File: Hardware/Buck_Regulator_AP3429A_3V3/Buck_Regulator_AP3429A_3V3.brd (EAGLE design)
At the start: 25.4 x 25.4 mm, 51 parts, among them J1 Screw Terminal, J2 POWER_JACKPOWER_JACK_SLOT_COM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, J3 Breakout Headers, U1 AP3429/A

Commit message: Added correct measurements
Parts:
- moved FRAME1 24.4 mm to (-14.0, -41.9)
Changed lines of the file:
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@@
 <layer number="45" name="Holes" color="7" fill="1" visible="yes" active="yes"/>
 <layer number="46" name="Milling" color="3" fill="1" visible="no" active="yes"/>
-<layer number="47" name="Measures" color="7" fill="1" visible="no" active="yes"/>
+<layer number="47" name="Measures" color="7" fill="1" visible="yes" active="yes"/>
 <layer number="48" name="Document" color="7" fill="1" visible="no" active="yes"/>
 <layer number="49" name="Reference" color="7" fill="1" visible="no" active="yes"/>
@@
 <wire x1="7.366" y1="10.541" x2="7.62" y2="10.287" width="0.1778" layer="21"/>
 <text x="20.447" y="0.508" size="1.778" layer="16" font="vector" ratio="15" rot="MR0">v01</text>
-<text x="16.51" y="-17.78" size="1.778" layer="51" font="vector" ratio="10" distance="15">M. Chodikov</text>
+<text x="12.7" y="-41.91" size="1.778" layer="51" font="vector" ratio="10" distance="15">M. Chodikov</text>
 <text x="5.08" y="46.99" size="1.778" layer="47" font="vector" ratio="15">Units in Inches</text>
 <wire x1="5.334" y1="11.176" x2="5.334" y2="10.414" width="0.2032" layer="22"/>
@@
 <rectangle x1="6.35" y1="3.81" x2="21.59" y2="16.51" layer="30" rot="R180"/>
 <wire x1="5.08" y1="11.43" x2="5.334" y2="11.176" width="0.2032" layer="22"/>
-<dimension x1="25.4" y1="25.4" x2="22.86" y2="25.4" x3="24.13" y3="29.21" textsize="1.778" textratio="15" layer="47" unit="inch"/>
-<dimension x1="2.54" y1="22.86" x2="0" y2="22.86" x3="1.27" y3="35.56" textsize="1.778" textratio="15" layer="47" unit="inch"/>
-<dimension x1="25.4" y1="25.4" x2="0" y2="25.4" x3="12.7" y3="40.64" textsize="1.778" textratio="15" layer="47" unit="inch"/>
-<dimension x1="2.54" y1="2.54" x2="2.54" y2="0" x3="-2.54" y3="1.27" textsize="1.778" textratio="15" layer="47" unit="inch"/>
-<dimension x1="2.54" y1="22.86" x2="2.54" y2="25.4" x3="-2.54" y3="24.13" textsize="1.778" textratio="15" layer="47" unit="inch"/>
-<dimension x1="3.683" y1="7.28" x2="3.81" y2="0" x3="-8.89" y3="3.64" textsize="1.778" textratio="15" layer="47" dtype="vertical" unit="inch"/>
-<dimension x1="3.683" y1="7.28" x2="3.81" y2="10.795" x3="-13.97" y3="9.0375" textsize="1.778" textratio="15" layer="47" dtype="vertical" unit="inch"/>
-<dimension x1="0" y1="25.4" x2="0" y2="0" x3="-20.32" y3="12.7" textsize="1.778" textratio="15" layer="47" unit="inch"/>
-<dimension x1="24.13" y1="7.493" x2="24.13" y2="0" x3="30.48" y3="3.7465" textsize="1.778" textratio="15" layer="47" unit="inch"/>
-<dimension x1="24.13" y1="7.62" x2="24.13" y2="10.16" x3="30.48" y3="8.89" textsize="1.778" textratio="15" layer="47" unit="inch"/>
+<dimension x1="2.54" y1="2.54" x2="0" y2="2.54" x3="1.27" y3="-3.81" textsize="1.778" textratio="15" layer="47" unit="inch"/>
+<dimension x1="3.683" y1="17.78" x2="0" y2="17.78" x3="1.8415" y3="-7.62" textsize="1.778" textratio="15" layer="47" unit="inch"/>
+<dimension x1="13.335" y1="24.003" x2="0" y2="24.003" x3="6.6675" y3="-12.7" textsize="1.778" textratio="15" layer="47" unit="inch"/>
+<dimension x1="22.86" y1="2.54" x2="0" y2="2.54" x3="11.43" y3="-17.78" textsize="1.778" textratio="15" layer="47" unit="inch"/>
+<dimension x1="24.13" y1="7.62" x2="0" y2="7.62" x3="12.065" y3="-21.59" textsize="1.778" textratio="15" layer="47" unit="inch"/>
+<dimension x1="25.4" y1="0" x2="0" y2="0" x3="12.7" y3="-26.67" textsize="1.778" textratio="15" layer="47" unit="inch"/>
+<dimension x1="3.683" y1="7.28" x2="3.81" y2="0" x3="-1.651" y3="3.64" textsize="1.778" textratio="15" layer="47" dtype="vertical" unit="inch"/>
+<dimension x1="24.13" y1="7.62" x2="24.13" y2="0" x3="-5.334" y3="3.81" textsize="1.778" textratio="15" layer="47" dtype="vertical" unit="inch"/>
+<dimension x1="25.4" y1="0" x2="24.13" y2="10.16" x3="-9.271" y3="5.08" textsize="1.778" textratio="15" layer="47" dtype="vertical" unit="inch"/>
+<dimension x1="3.683" y1="10.795" x2="3.683" y2="0" x3="-12.827" y3="5.3975" textsize="1.778" textratio="15" layer="47" dtype="vertical" unit="inch"/>
+<dimension x1="2.54" y1="2.54" x2="2.54" y2="0" x3="-16.51" y3="1.27" textsize="1.778" textratio="15" layer="47" dtype="vertical" unit="inch"/>
+<dimension x1="2.54" y1="22.86" x2="2.54" y2="0" x3="-20.32" y3="11.43" textsize="1.778" textratio="15" layer="47" dtype="vertical" unit="inch"/>
+<dimension x1="13.335" y1="24.003" x2="13.97" y2="0" x3="-25.4" y3="12.0015" textsize="1.778" textratio="15" layer="47" dtype="vertical" unit="inch"/>
+<dimension x1="0" y1="0" x2="0" y2="25.4" x3="-29.21" y3="12.7" textsize="1.778" textratio="15" layer="47" dtype="vertical" unit="inch"/>
+<text x="-25.4" y="-12.7" size="1.778" layer="47" font="vector" ratio="15">Units in Inches</text>
 </plain>
 <attributes>
@@
 <element name="FD3" library="SparkFun-Aesthetics" package="FIDUCIAL-MICRO" value="FIDUCIALUFIDUCIAL" x="0.762" y="24.638" smashed="yes" rot="MR0"/>
 <element name="FD4" library="SparkFun-Aesthetics" package="FIDUCIAL-MICRO" value="FIDUCIALUFIDUCIAL" x="0.762" y="24.638" smashed="yes"/>
-<element name="FRAME1" library="SparkFun-Aesthetics" package="CREATIVE_COMMONS" value="FRAME-LEDGER" x="-10.16" y="-17.78" smashed="yes">
-<attribute name="DESIGNER" value="M. Chodikov" x="69.85" y="-30.48" size="1.778" layer="27" display="off"/>
-<attribute name="REV" value="v01" x="69.85" y="-30.48" size="1.778" layer="27" display="off"/>
+<element name="FRAME1" library="SparkFun-Aesthetics" package="CREATIVE_COMMONS" value="FRAME-LEDGER" x="-13.97" y="-41.91" smashed="yes">
+<attribute name="DESIGNER" value="M. Chodikov" x="66.04" y="-54.61" size="1.778" layer="27" display="off"/>
+<attribute name="REV" value="v01" x="66.04" y="-54.61" size="1.778" layer="27" display="off"/>
 </element>
 <element name="L1" library="SparkFun-Coils" package="INDUCTOR_4X4MM" value="2.2μH" x="16.256" y="8.509" smashed="yes">

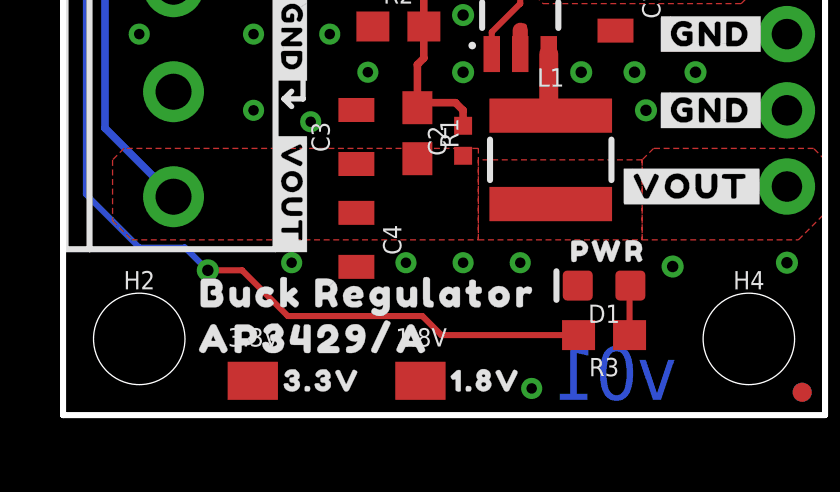
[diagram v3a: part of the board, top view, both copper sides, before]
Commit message: Further design review changes - v01
Added selective solder path to Document layer for the terminal block; moved the silkscreen name on the front to not be covered by the mounting hole anymore when a user uses a screw; nudges the LED power trace over for better GND connection; added measures to thermal pad (in reference to bottom right, and for the size)
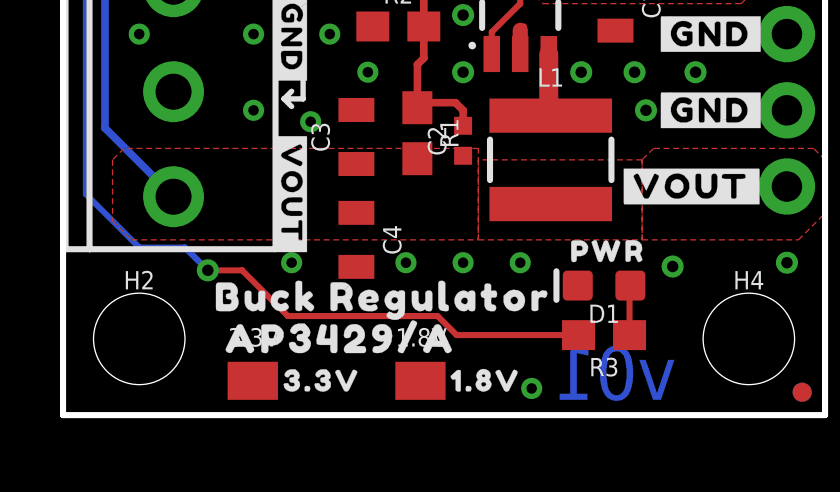
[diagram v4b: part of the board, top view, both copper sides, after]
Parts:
- moved U$3 0.89 mm to (9.27, 2.54)
- moved U$2 0.52 mm to (10.7, 3.94)
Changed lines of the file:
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@@
 <drawing>
 <settings>
-<setting alwaysvectorfont="no"/>
+<setting alwaysvectorfont="yes"/>
 <setting verticaltext="up"/>
 </settings>
@@
 <layer number="28" name="bValues" color="7" fill="1" visible="no" active="yes"/>
 <layer number="29" name="tStop" color="7" fill="3" visible="no" active="yes"/>
-<layer number="30" name="bStop" color="7" fill="6" visible="no" active="yes"/>
+<layer number="30" name="bStop" color="7" fill="6" visible="yes" active="yes"/>
 <layer number="31" name="tCream" color="7" fill="4" visible="no" active="yes"/>
 <layer number="32" name="bCream" color="7" fill="5" visible="no" active="yes"/>
@@
 <layer number="46" name="Milling" color="3" fill="1" visible="no" active="yes"/>
 <layer number="47" name="Measures" color="7" fill="1" visible="yes" active="yes"/>
-<layer number="48" name="Document" color="7" fill="1" visible="no" active="yes"/>
+<layer number="48" name="Document" color="7" fill="1" visible="yes" active="yes"/>
 <layer number="49" name="Reference" color="7" fill="1" visible="no" active="yes"/>
 <layer number="50" name="dxf" color="7" fill="1" visible="no" active="no"/>
@@
 <text x="20.447" y="0.508" size="1.778" layer="16" font="vector" ratio="15" rot="MR0">v01</text>
 <text x="12.7" y="-41.91" size="1.778" layer="51" font="vector" ratio="10" distance="15">M. Chodikov</text>
-<text x="5.08" y="46.99" size="1.778" layer="47" font="vector" ratio="15">Units in Inches</text>
 <wire x1="5.334" y1="11.176" x2="5.334" y2="10.414" width="0.2032" layer="22"/>
 <wire x1="5.334" y1="10.414" x2="4.826" y2="10.414" width="0.2032" layer="22"/>
@@
 <dimension x1="2.54" y1="2.54" x2="0" y2="2.54" x3="1.27" y3="-3.81" textsize="1.778" textratio="15" layer="47" unit="inch"/>
 <dimension x1="3.683" y1="17.78" x2="0" y2="17.78" x3="1.8415" y3="-7.62" textsize="1.778" textratio="15" layer="47" unit="inch"/>
-<dimension x1="13.335" y1="24.003" x2="0" y2="24.003" x3="6.6675" y3="-12.7" textsize="1.778" textratio="15" layer="47" unit="inch"/>
-<dimension x1="22.86" y1="2.54" x2="0" y2="2.54" x3="11.43" y3="-17.78" textsize="1.778" textratio="15" layer="47" unit="inch"/>
-<dimension x1="24.13" y1="7.62" x2="0" y2="7.62" x3="12.065" y3="-21.59" textsize="1.778" textratio="15" layer="47" unit="inch"/>
-<dimension x1="25.4" y1="0" x2="0" y2="0" x3="12.7" y3="-26.67" textsize="1.778" textratio="15" layer="47" unit="inch"/>
 <dimension x1="3.683" y1="7.28" x2="3.81" y2="0" x3="-1.651" y3="3.64" textsize="1.778" textratio="15" layer="47" dtype="vertical" unit="inch"/>
 <dimension x1="24.13" y1="7.62" x2="24.13" y2="0" x3="-5.334" y3="3.81" textsize="1.778" textratio="15" layer="47" dtype="vertical" unit="inch"/>
 <dimension x1="25.4" y1="0" x2="24.13" y2="10.16" x3="-9.271" y3="5.08" textsize="1.778" textratio="15" layer="47" dtype="vertical" unit="inch"/>
 <dimension x1="3.683" y1="10.795" x2="3.683" y2="0" x3="-12.827" y3="5.3975" textsize="1.778" textratio="15" layer="47" dtype="vertical" unit="inch"/>
-<dimension x1="2.54" y1="2.54" x2="2.54" y2="0" x3="-16.51" y3="1.27" textsize="1.778" textratio="15" layer="47" dtype="vertical" unit="inch"/>
-<dimension x1="2.54" y1="22.86" x2="2.54" y2="0" x3="-20.32" y3="11.43" textsize="1.778" textratio="15" layer="47" dtype="vertical" unit="inch"/>
-<dimension x1="13.335" y1="24.003" x2="13.97" y2="0" x3="-25.4" y3="12.0015" textsize="1.778" textratio="15" layer="47" dtype="vertical" unit="inch"/>
-<dimension x1="0" y1="0" x2="0" y2="25.4" x3="-29.21" y3="12.7" textsize="1.778" textratio="15" layer="47" dtype="vertical" unit="inch"/>
 <text x="-25.4" y="-12.7" size="1.778" layer="47" font="vector" ratio="15">Units in Inches</text>
+<wire x1="3.048" y1="16.891" x2="3.048" y2="6.35" width="5.9944" layer="48"/>
+<wire x1="3.048" y1="6.35" x2="0" y2="3.302" width="5.9944" layer="48"/>
+<dimension x1="6.35" y1="3.81" x2="0" y2="3.81" x3="3.175" y3="-11.43" textsize="1.778" textratio="15" layer="47" unit="inch"/>
+<dimension x1="13.335" y1="24.003" x2="0" y2="24.003" x3="6.6675" y3="-16.51" textsize="1.778" textratio="15" layer="47" unit="inch"/>
+<dimension x1="22.86" y1="2.54" x2="0" y2="2.54" x3="11.43" y3="-21.59" textsize="1.778" textratio="15" layer="47" unit="inch"/>
+<dimension x1="24.13" y1="7.62" x2="0" y2="7.62" x3="12.065" y3="-25.4" textsize="1.778" textratio="15" layer="47" unit="inch"/>
+<dimension x1="25.4" y1="0" x2="0" y2="0" x3="12.7" y3="-29.21" textsize="1.778" textratio="15" layer="47" unit="inch"/>
+<dimension x1="6.35" y1="3.81" x2="6.35" y2="0" x3="-16.51" y3="1.905" textsize="1.778" textratio="15" layer="47" unit="inch"/>
+<dimension x1="2.54" y1="2.54" x2="2.54" y2="0" x3="-20.32" y3="1.27" textsize="1.778" textratio="15" layer="47" unit="inch"/>
+<dimension x1="2.54" y1="22.86" x2="2.54" y2="0" x3="-24.13" y3="11.43" textsize="1.778" textratio="15" layer="47" unit="inch"/>
+<dimension x1="13.335" y1="24.003" x2="13.335" y2="0" x3="-27.94" y3="12.0015" textsize="1.778" textratio="15" layer="47" unit="inch"/>
+<dimension x1="0" y1="0" x2="0" y2="25.4" x3="-31.75" y3="12.7" textsize="1.778" textratio="15" layer="47" unit="inch"/>
+<dimension x1="21.59" y1="3.81" x2="21.59" y2="16.51" x3="30.48" y3="10.16" textsize="1.778" textratio="15" layer="47" unit="inch"/>
+<dimension x1="6.35" y1="16.51" x2="21.59" y2="16.51" x3="13.97" y3="35.56" textsize="1.778" textratio="15" layer="47" unit="inch"/>
 </plain>
 <attributes>
@@
 <attribute name="VALUE" x="22.098" y="19.05" size="0.6096" layer="27" font="vector" ratio="20" rot="R270"/>
 </element>
-<element name="U$2" library="output" package="BUCK_REGULATOR24" value="" x="10.16" y="4.064" smashed="yes"/>
-<element name="U$3" library="output" package="AP3429#A25" value="" x="8.382" y="2.54" smashed="yes"/>
+<element name="U$2" library="output" package="BUCK_REGULATOR24" value="" x="10.668" y="3.937" smashed="yes"/>
+<element name="U$3" library="output" package="AP3429#A25" value="" x="9.271" y="2.54" smashed="yes"/>
 <element name="U$4" library="output" package="#VOUT#3431" value="" x="20.955" y="7.62" smashed="yes"/>
 <element name="U$5" library="output" package="#GND#3432" value="" x="21.59" y="10.16" smashed="yes"/>
@@
 <wire x1="4.8387" y1="20.8407" x2="4.318" y2="20.32" width="0.2032" layer="16"/>
 <wire x1="4.318" y1="20.32" x2="1.651" y2="20.32" width="0.2032" layer="16"/>
-<wire x1="11.977" y1="3.302" x2="12.612" y2="2.667" width="0.2032" layer="1"/>
-<wire x1="11.977" y1="3.302" x2="7.493" y2="3.302" width="0.2032" layer="1"/>
+<wire x1="12.485" y1="3.302" x2="13.12" y2="2.667" width="0.2032" layer="1"/>
+<wire x1="12.485" y1="3.302" x2="7.493" y2="3.302" width="0.2032" layer="1"/>
 <via x="4.826" y="4.826" extent="1-16" drill="0.381"/>
 <wire x1="4.826" y1="4.826" x2="5.969" y2="4.826" width="0.2032" layer="1"/>
@@
 <wire x1="4.064" y1="5.588" x2="2.54" y2="5.588" width="0.2032" layer="16"/>
 <contactref element="R3" pad="2"/>
-<wire x1="12.612" y1="2.667" x2="17.184" y2="2.667" width="0.2032" layer="1"/>
+<wire x1="13.12" y1="2.667" x2="17.184" y2="2.667" width="0.2032" layer="1"/>
 </signal>
 <signal name="N$4">

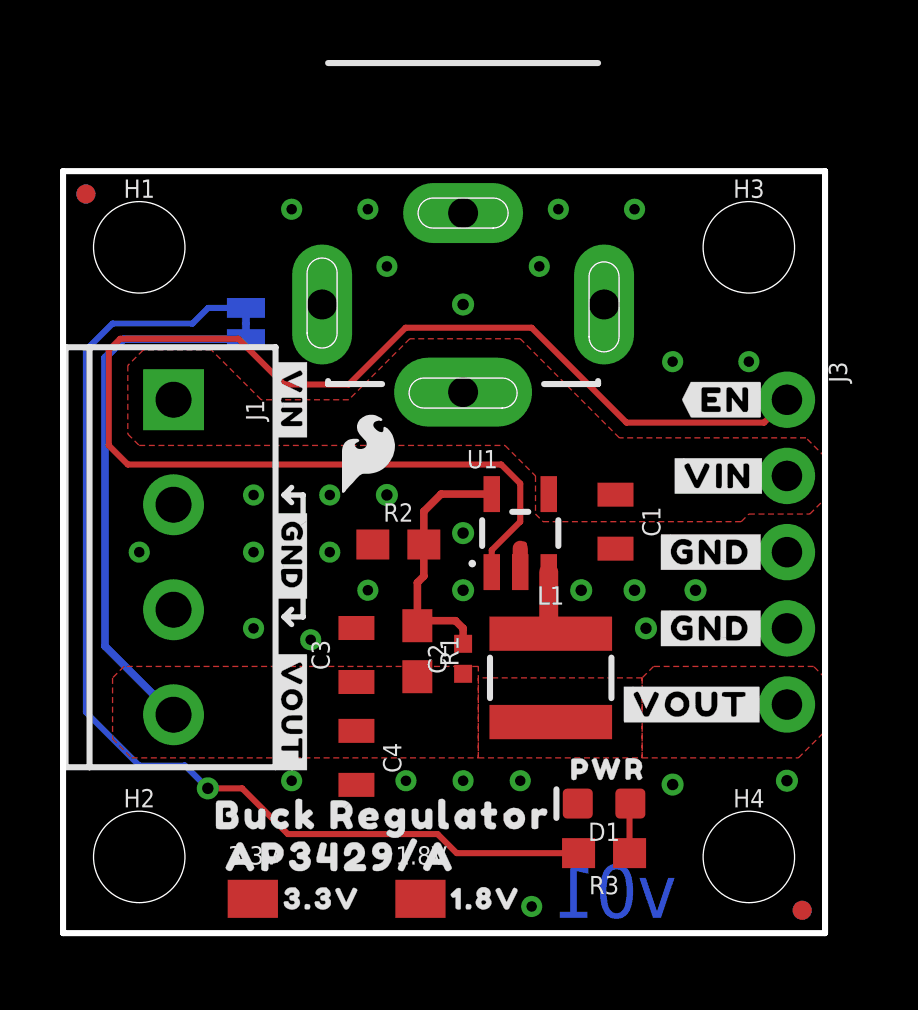
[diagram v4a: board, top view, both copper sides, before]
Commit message: Updated files for design review
Changed the version number on the board file to be V10 instead of V01, then changed the footprint of the power jack on each side of the board to swap the sides of the exposed copper on the groundbreak pins for easier soldering.
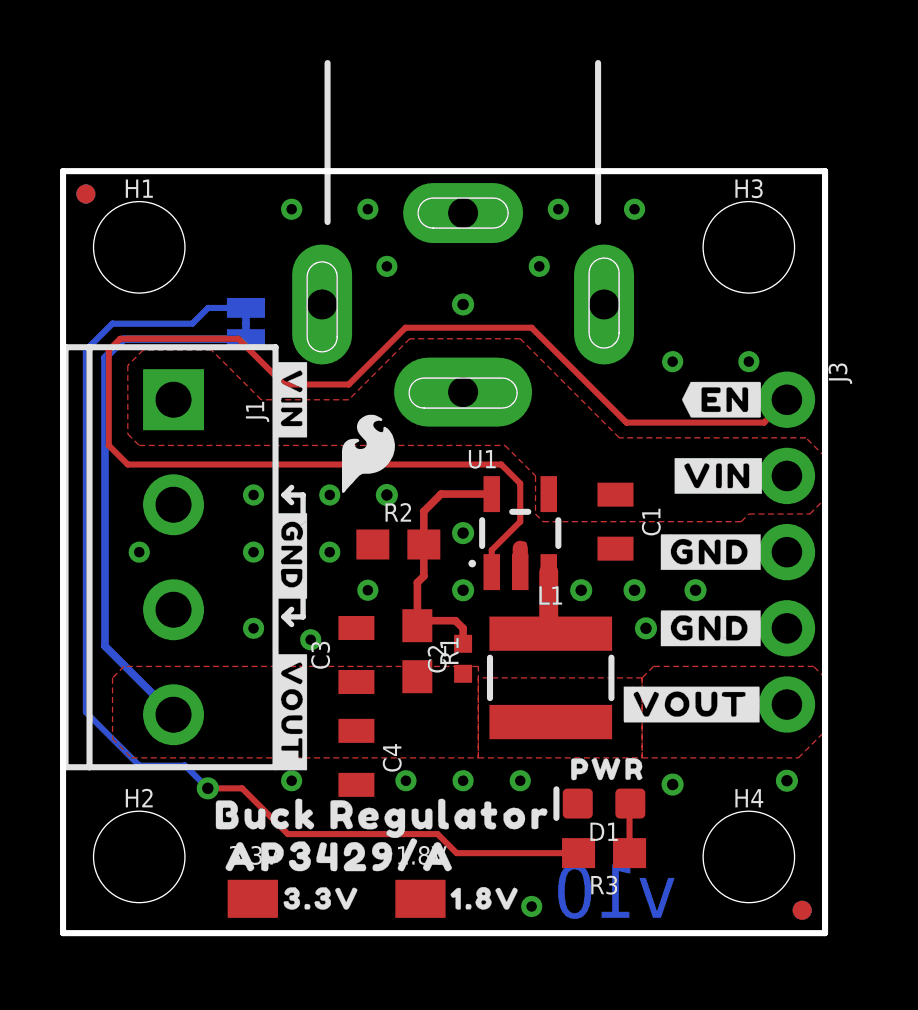
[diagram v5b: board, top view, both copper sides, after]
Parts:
- flipped J2 to the bottom
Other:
- board text added: "v10"
- board text removed: "v01"
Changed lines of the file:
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@@
 <layer number="28" name="bValues" color="7" fill="1" visible="no" active="yes"/>
 <layer number="29" name="tStop" color="7" fill="3" visible="no" active="yes"/>
-<layer number="30" name="bStop" color="7" fill="6" visible="yes" active="yes"/>
+<layer number="30" name="bStop" color="7" fill="6" visible="no" active="yes"/>
 <layer number="31" name="tCream" color="7" fill="4" visible="no" active="yes"/>
 <layer number="32" name="bCream" color="7" fill="5" visible="no" active="yes"/>
@@
 <layer number="45" name="Holes" color="7" fill="1" visible="yes" active="yes"/>
 <layer number="46" name="Milling" color="3" fill="1" visible="no" active="yes"/>
-<layer number="47" name="Measures" color="7" fill="1" visible="yes" active="yes"/>
-<layer number="48" name="Document" color="7" fill="1" visible="yes" active="yes"/>
+<layer number="47" name="Measures" color="7" fill="1" visible="no" active="yes"/>
+<layer number="48" name="Document" color="7" fill="1" visible="no" active="yes"/>
 <layer number="49" name="Reference" color="7" fill="1" visible="no" active="yes"/>
 <layer number="50" name="dxf" color="7" fill="1" visible="no" active="no"/>
@@
 <wire x1="7.366" y1="10.541" x2="7.62" y2="10.795" width="0.1778" layer="21"/>
 <wire x1="7.366" y1="10.541" x2="7.62" y2="10.287" width="0.1778" layer="21"/>
-<text x="20.447" y="0.508" size="1.778" layer="16" font="vector" ratio="15" rot="MR0">v01</text>
+<text x="20.447" y="0.508" size="1.778" layer="16" font="vector" ratio="15" rot="MR0">v10</text>
 <text x="12.7" y="-41.91" size="1.778" layer="51" font="vector" ratio="10" distance="15">M. Chodikov</text>
 <wire x1="5.334" y1="11.176" x2="5.334" y2="10.414" width="0.2032" layer="22"/>
@@
 <attribute name="VALUE" x="8.89" y="5.842" size="0.6096" layer="27" font="vector" ratio="20" rot="R270" align="top-center"/>
 </element>
-<element name="J2" library="SparkFun-Connectors" package="POWER_JACK_PTH_SLOT_BOTH" value="POWER_JACKPOWER_JACK_SLOT_COMBO" x="13.335" y="24.003" smashed="yes" rot="R90"/>
 <element name="U$16" library="output" package="BUCK_REGULATOR_AP3429#A3453" value="" x="1.524" y="12.827" smashed="yes" rot="MR90"/>
 <element name="R1" library="SparkFun-Resistors" package="0603" value="453k" x="11.811" y="9.398" smashed="yes" rot="R270">
@@
 <attribute name="VALUE" x="18.034" y="3.429" size="0.6096" layer="27" font="vector" ratio="20" rot="R180" align="top-center"/>
 </element>
+<element name="J2" library="SparkFun-Connectors" package="POWER_JACK_PTH_SLOT_BOTH" value="POWER_JACKPOWER_JACK_SLOT_COMBO" x="13.335" y="24.003" smashed="yes" rot="MR90"/>
 </elements>
 <signals>
@@
 <contactref element="J1" pad="1"/>
 <contactref element="C1" pad="1"/>
-<contactref element="J2" pad="PWR"/>
 <polygon width="0.2032" layer="1" isolate="0.3048">
 <vertex x="2.159" y="18.923"/>
@@
 <vertex x="2.667" y="19.431"/>
 </polygon>
+<contactref element="J2" pad="PWR"/>
 </signal>
 <signal name="GND">
@@
 <contactref element="C3" pad="2"/>
 <contactref element="C4" pad="2"/>
-<contactref element="J2" pad="GND"/>
 <polygon width="0.2032" layer="1" isolate="0.3048" rank="2">
 <vertex x="0" y="0"/>
@@
 <via x="10.16" y="24.13" extent="1-16" drill="0.35"/>
 <contactref element="R2" pad="1"/>
+<contactref element="J2" pad="GND"/>
 </signal>
 <signal name="N$1">
@@
 </signals>
 <mfgpreviewcolors>
-<mfgpreviewcolor name="soldermaskcolor" color="0xC8000000"/>
+<mfgpreviewcolor name="soldermaskcolor" color="0xC8FF0000"/>
 <mfgpreviewcolor name="silkscreencolor" color="0xFFFEFEFE"/>
 <mfgpreviewcolor name="backgroundcolor" color="0xFF282828"/>
